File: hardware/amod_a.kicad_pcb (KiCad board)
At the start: 4 copper layers, 100 x 100 mm, 189 parts, among them J1001 SMA, J1002 SMA, J1003 SMA, J1004 SMA, J101 USB-C, J102 rails, J1101 SMA, J1102 TX, J1103 RX, J1104 Pmod, J1201 SMA, J1202 SMA, J1203 SPK, J1204 MIC, J201 SMA, J202 SMA, J301 SMA, J302 SMA, J401 SMA, J402 SMA, J501 SMA, J502 HB100, J601 SMA, J701 SMA, J702 SMA, J801 SMA, J901 SMA, J902 SMA, J903 SMA, Q1001 AO3401A, Q1101 AO3401A, Q1201 AO3401A, Q201 AO3401A, Q301 AO3401A, Q401 AO3401A, Q501 AO3401A, Q601 AO3401A, Q701 AO3401A, Q801 AO3401A, Q802 AO3400A, Q901 AO3401A, SW1001 ON, SW1002 DIP4, SW1101 ON, SW1201 ON, SW201 ON, SW301 ON, SW401 ON, SW501 ON, SW601 ON, SW701 ON, SW801 ON, SW901 ON, U1001 OPA810, U1002 OPA810, U101 LM2664, U102 3.3V, U1101 DRV8837, U1102 OPA810, U1201 PAM8302A, U1202 OPA810, U201 OPA810, U301 OPA810, U401 OPA847, U501 OPA810, U601 TLV3501, U701 74HC4046A, U801 TMP235, U901 MC1496

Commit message: One letter per board, tiles in lower case: AMOD-P2 is AMOD-N (n1-n11), RF-MOD-2 is IQ-MOD (q1-q11), PhMOD's tiles h1-h10
Jason, Prompt 19: "If we can have a nice, well justified single-letter designator for each board, it would make
everything much more clear", and "d11, q11, and c11 don't look like obvious electronics or PCB things".

- p passive, n networks (AMOD-P2's P14, P16-P25), a active, r radio, h PhMOD (Y1-Y10), q quadrature (RF-MOD-2's X1-X11);
  c, m and b are taken for the conversion, motor and brushless boards to come.  PLAN.md section 13 has the table and
  the reasons (no letter moves to another board, no retired name is reused, no s: s11 is the reflection coefficient).
- Every tile name in lower case on the silk, in the code (Tile ids, BACK/BACK_PLOTS/DOCS keys, the nets built on them),
  the handbooks, README, DOA lists, KIT, PLAN and the review brief; pin names (USB-C A1...), the 4046's R1/C1, nets
  named N1/P1, part numbers ending -R7 and the paper size A1 left alone.  tiles.dump refuses a tile not named
  <letter><n>, a number twice, and a BACK key for a tile that does not exist.
- Board and file renames: boards/amod_n.py, boards/iq_mod.py, docs/DOA_amod_n.md, docs/DOA_iq_mod.md, the handbooks,
  the generated hardware, outputs and pictures.  Silk nudged where a lower-case p or q hung onto the line below.
- All six boards rebuilt: ERC 0, DRC 0, every check.

Co-Authored-By: Claude Opus 5.5 <noreply@anthropic.com>
Claude-Session: https://claude.ai/code/session_01RKeoKvFFzjk3cEBLCXXHnB
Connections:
- net /A10_FB renamed /a10_FB
- net /A10_G renamed /a10_G
- net /A10_IN renamed /a10_IN
- net /A10_OUT renamed /a10_OUT
- net /A10_OUT_A renamed /a10_OUT_A
- net /A10_R1 renamed /a10_R1
- net /A10_R2 renamed /a10_R2
- net /A10_R3 renamed /a10_R3
- net /A10_R4 renamed /a10_R4
- net /A10_VS renamed /a10_VS
- net /A10_X renamed /a10_X
- net /A10_XF renamed /a10_XF
- net /A10_XO renamed /a10_XO
- net /A11_FB renamed /a11_FB
- net /A11_G renamed /a11_G
- net /A11_IN renamed /a11_IN
- net /A11_OUT renamed /a11_OUT
- net /A11_OUT1 renamed /a11_OUT1
- net /A11_OUT2 renamed /a11_OUT2
- net /A11_OUT_A renamed /a11_OUT_A
- net /A11_RXA renamed /a11_RXA
- net /A11_VS renamed /a11_VS
- net /A12_AIN renamed /a12_AIN
- net /A12_BYP renamed /a12_BYP
- net /A12_FB renamed /a12_FB
- net /A12_G renamed /a12_G
- net /A12_IN renamed /a12_IN
- net /A12_INM renamed /a12_INM
- net /A12_MICP renamed /a12_MICP
- net /A12_NODE renamed /a12_NODE
- net /A12_OUT renamed /a12_OUT
- net /A12_OUT_A renamed /a12_OUT_A
- net /A12_VOM renamed /a12_VOM
- net /A12_VOP renamed /a12_VOP
- net /A12_VS renamed /a12_VS
- net /A1_CAPN renamed /a1_CAPN
- net /A1_CAPP renamed /a1_CAPP
- net /A1_CC1 renamed /a1_CC1
- net /A1_CC2 renamed /a1_CC2
- net /A1_LEDG renamed /a1_LEDG
- net /A1_LEDR renamed /a1_LEDR
- net /A1_VBUS renamed /a1_VBUS
- net /A2_FB renamed /a2_FB
- net /A2_G renamed /a2_G
- net /A2_IN renamed /a2_IN
- net /A2_OUT renamed /a2_OUT
- net /A2_OUT_A renamed /a2_OUT_A
- net /A2_VS renamed /a2_VS
- net /A3_FB renamed /a3_FB
- net /A3_G renamed /a3_G
- net /A3_IN renamed /a3_IN
- net /A3_OUT renamed /a3_OUT
- net /A3_OUT_A renamed /a3_OUT_A
- net /A3_VS renamed /a3_VS
- net /A4_FB renamed /a4_FB
- net /A4_G renamed /a4_G
- net /A4_IN renamed /a4_IN
- net /A4_OUT renamed /a4_OUT
- net /A4_OUT_A renamed /a4_OUT_A
- net /A4_VS renamed /a4_VS
- net /A5_FB renamed /a5_FB
- net /A5_G renamed /a5_G
- net /A5_IF renamed /a5_IF
- net /A5_IN renamed /a5_IN
- net /A5_OUT renamed /a5_OUT
- net /A5_OUT_A renamed /a5_OUT_A
- net /A5_VS renamed /a5_VS
- net /A6_G renamed /a6_G
- net /A6_IN renamed /a6_IN
- net /A6_NODE renamed /a6_NODE
- net /A6_VREF renamed /a6_VREF
- net /A6_VS renamed /a6_VS
- net /A7_C1A renamed /a7_C1A
- net /A7_C1B renamed /a7_C1B
- net /A7_G renamed /a7_G
- net /A7_IN renamed /a7_IN
- net /A7_INA renamed /a7_INA
- net /A7_NODE renamed /a7_NODE
- net /A7_OUT renamed /a7_OUT
- net /A7_PC2 renamed /a7_PC2
- net /A7_R1 renamed /a7_R1
- net /A7_SIG renamed /a7_SIG
- net /A7_VCO_A renamed /a7_VCO_A
- net /A7_VS renamed /a7_VS
- net /A8_DRN renamed /a8_DRN
- net /A8_G renamed /a8_G
- net /A8_HTR renamed /a8_HTR
- net /A8_OUT renamed /a8_OUT
- net /A8_VS renamed /a8_VS
- net /A9_BIAS renamed /a9_BIAS
- net /A9_CARA renamed /a9_CARA
- net /A9_CARB renamed /a9_CARB
- net /A9_CB renamed /a9_CB
- net /A9_G renamed /a9_G
- net /A9_GAIN2 renamed /a9_GAIN2
- net /A9_GAIN3 renamed /a9_GAIN3
- net /A9_IF renamed /a9_IF
- net /A9_LO renamed /a9_LO
- net /A9_OUTA renamed /a9_OUTA
- net /A9_OUTB renamed /a9_OUTB
- net /A9_RF renamed /a9_RF
- net /A9_SIGA renamed /a9_SIGA
- net /A9_SIGB renamed /a9_SIGB
- net /A9_VS renamed /a9_VS
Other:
- board text added: "a1"
- board text added: "a1 Power"
- board text added: "a10"
- board text added: "a10 Impedance"
- board text added: "a11"
- board text added: "a11 Ultrasound"
- board text added: "a12"
- board text added: "a12 Audio"
- board text added: "a2"
- board text added: "a2 x10"
- board text added: "a3"
- board text added: "a3 x100"
- board text added: "a4"
- board text added: "a4 LNA"
- board text added: "a5"
- board text added: "a5 Doppler"
- board text added: "a6"
- board text added: "a6 1-bit ADC"
- board text added: "a7"
- board text added: "a7 PLL 4046"
- board text added: "a8"
- board text added: "a8 Heat"
- board text added: "a9"
- board text added: "a9 Mixer"
- board text removed: "A1"
- board text removed: "A1 Power"
- board text removed: "A10"
- board text removed: "A10 Impedance"
- board text removed: "A11"
- board text removed: "A11 Ultrasound"
- board text removed: "A12"
- board text removed: "A12 Audio"
- board text removed: "A2"
- board text removed: "A2 x10"
- board text removed: "A3"
- board text removed: "A3 x100"
- board text removed: "A4"
- board text removed: "A4 LNA"
- board text removed: "A5"
- board text removed: "A5 Doppler"
- board text removed: "A6"
- board text removed: "A6 1-bit ADC"
- board text removed: "A7"
- board text removed: "A7 PLL 4046"
- board text removed: "A8"
- board text removed: "A8 Heat"
- board text removed: "A9"
- board text removed: "A9 Mixer"

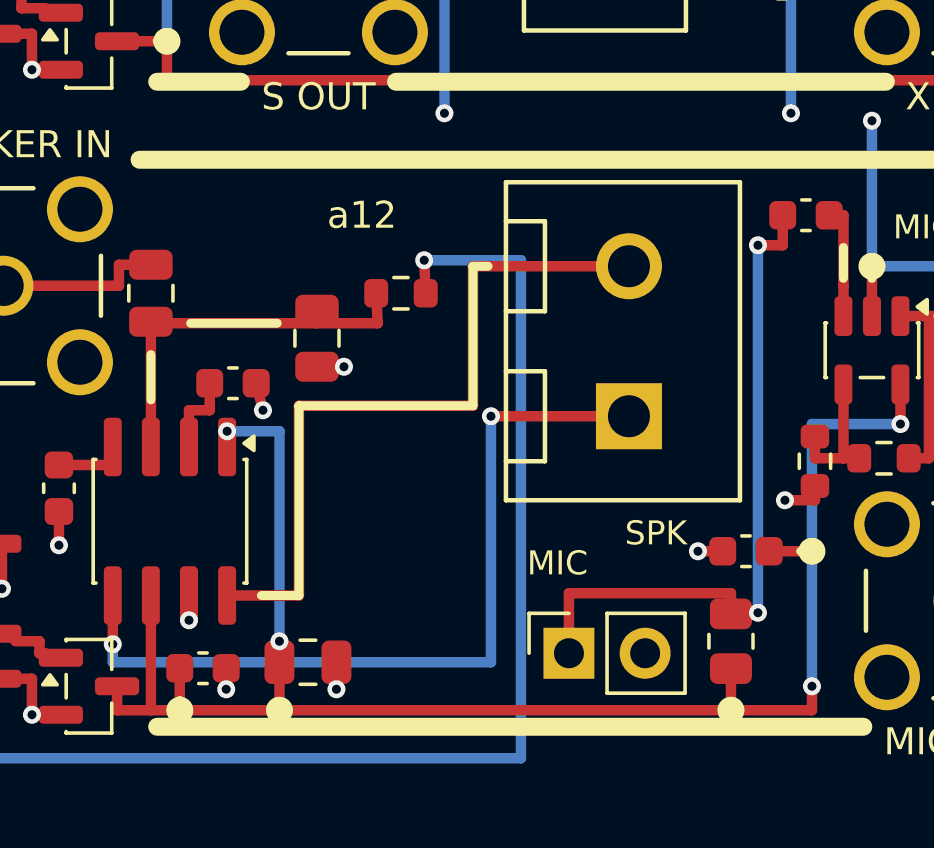
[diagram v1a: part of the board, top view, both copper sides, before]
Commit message: Pre-order checks from CLAUDE_PCB.md's new lessons (Prompt 21): the KF301 terminals turned for their wire openings (CPL +180, body 3.7 / 4.0, a wire-face check), four oversold parts swapped (27R, 6.8k, 220n, OPA847IDBVT at its own +180), fourteen vias moved out of SMD pads (check_layout.py gates it and RF detours), 200-250 mW terminations, assembly drawings from Fab and silk fitted to Letter (fit_pdf.py from CostasLink), the stock gate on JLCPCB's free count, electrolytics in the rotation check, the RF gates surveyed (rf_extract.py, rf_survey.py) and written into the DOA lists; all nine boards rebuilt: ERC 0, DRC 0, every check
Co-Authored-By: Claude Opus 5.5 <noreply@anthropic.com>
Claude-Session: https://claude.ai/code/session_01RKeoKvFFzjk3cEBLCXXHnB
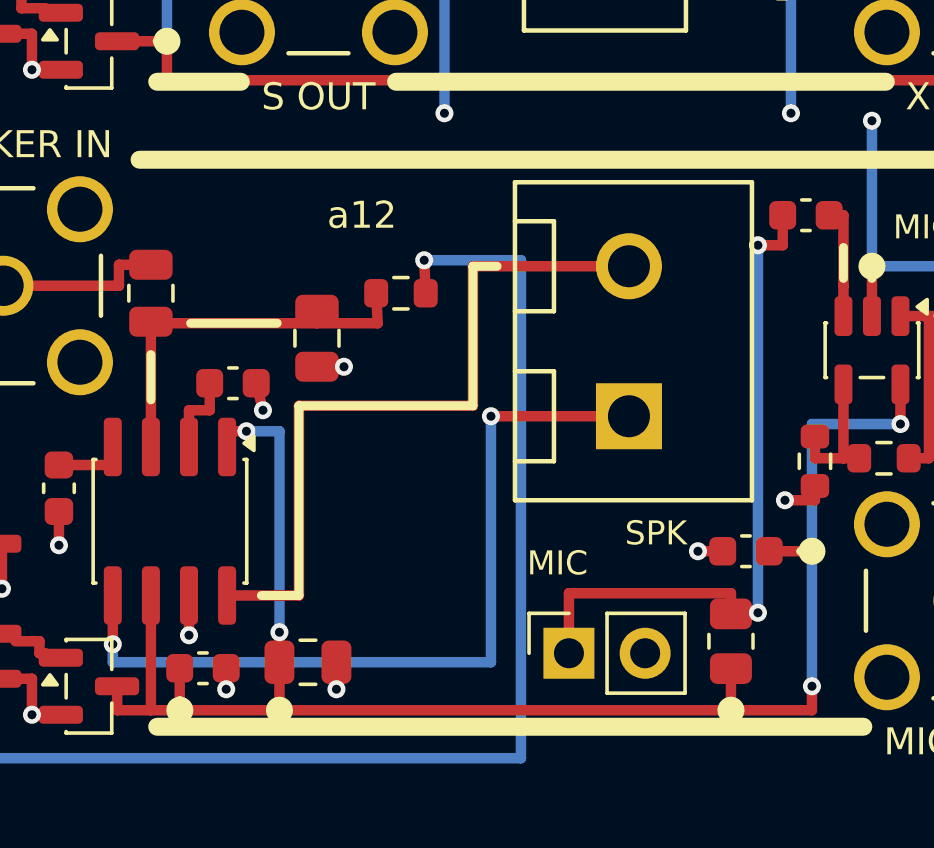
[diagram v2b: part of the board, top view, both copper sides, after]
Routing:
- net GND: track 113.5 -> 114.0 mm

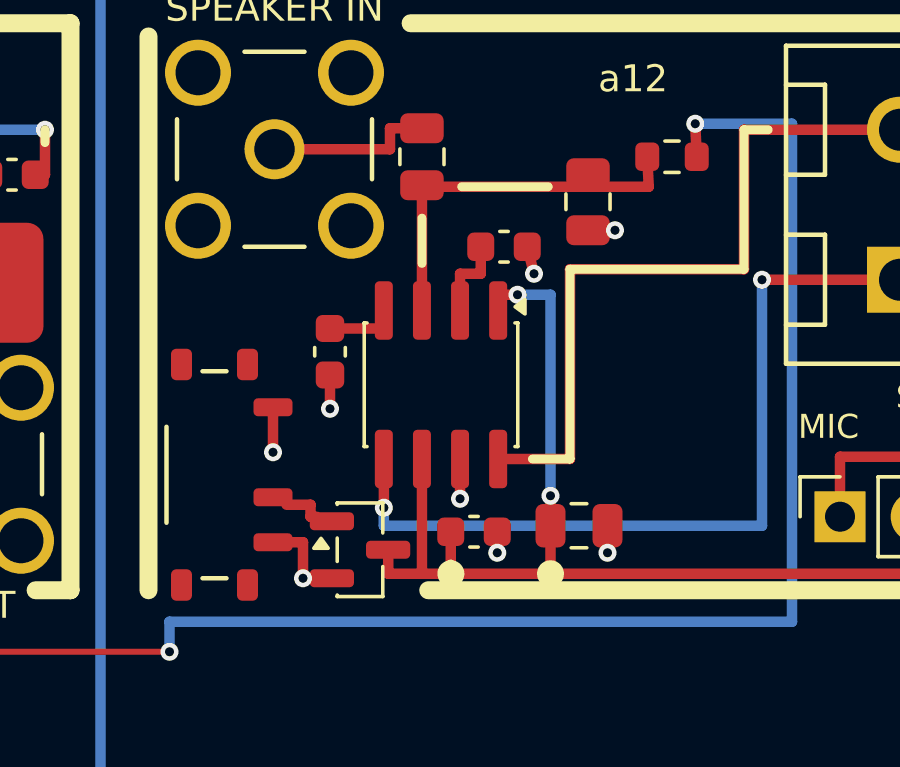
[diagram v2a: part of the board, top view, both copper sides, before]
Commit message: AMOD-A's PAM8302 on its real MSOP-8 (Prompt 22: JLCPCB's preview showed the MSOP-8 on our SOIC-8 pads; a12 re-laid, pin 2 NC); check_overlay.py lays JLCPCB's drawing on our pads in every build (a wrong package with the right pin order failed nothing before); check_pinouts pairs EasyEDA's names by the printed pin number; the order steps say Specify Stackup No (JLC04161H-7628's construction), the via size and Plugged; the chat log
Co-Authored-By: Claude Opus 5.5 <noreply@anthropic.com>
Claude-Session: https://claude.ai/code/session_01RKeoKvFFzjk3cEBLCXXHnB
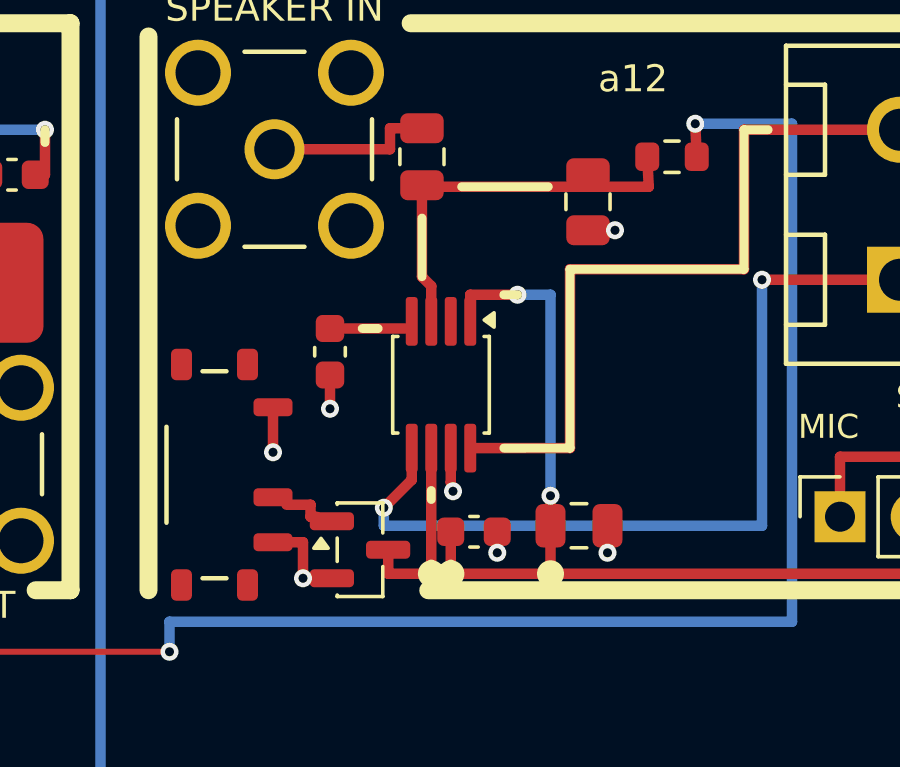
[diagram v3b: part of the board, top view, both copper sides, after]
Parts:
- removed C1209: 100n, Capacitor_SMD:C_0603_1608Metric
- C1204, C1207: value 1u -> 100n
- C1205: value 100n -> 10u; footprint Capacitor_SMD:C_0603_1608Metric -> Capacitor_SMD:C_0805_2012Metric
- C1206: value 10u -> 1u; footprint Capacitor_SMD:C_0805_2012Metric -> Capacitor_SMD:C_0603_1608Metric
- U1201: footprint Package_SO:SOIC-8_3.9x4.9mm_P1.27mm -> Package_SO:MSOP-8_3x3mm_P0.65mm
- moved C1206 22.3 mm to (82.2, 74.7)
- moved C1208 12.4 mm to (80.2, 85.8)
- moved C1204 9.55 mm to (62.1, 89.8)
- moved C1207 8.15 mm to (89.8, 77.8)
- moved C1205 3.51 mm to (65.7, 89.5)
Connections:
- C1204 pad 1: /a12_BYP -> /a12_VS
- C1206 pad 1: /a12_VS -> /a12_MICP
- C1206 pad 2: GND -> /a12_IN
- C1207 pad 1: /a12_MICP -> GND
- C1207 pad 2: /a12_IN -> -5V
- C1208 pad 2: -5V -> /a12_VS
- U1201 pad 2: /a12_BYP -> unconnected-(U1201-NC-Pad2)
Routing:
- net /a12_BYP: track 2.81 -> 0.00 mm
- net /a12_VS: track 57.4 -> 59.0 mm
- net GND: track 114.0 -> 113.2 mm, vias 85 -> 84
- net /a12_VOP: track 27.6 -> 28.4 mm
- net /a12_INM: track 2.39 -> 2.96 mm
- net /a12_VOM: track 24.4 -> 24.9 mm
